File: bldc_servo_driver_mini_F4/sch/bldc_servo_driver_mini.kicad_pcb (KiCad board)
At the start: 4 copper layers, 35 x 40 mm, 68 parts, among them IC1 ST730MR, IC2 LDK320AM50R, IC3 TLT9251VLEXUMA1, J1 1-2328702-0, J2 Conn_01x04, J3 Conn_01x04, J4 Conn_01x06, J5 Conn_01x03, J6 Conn_01x02, J7 DF65-3P-1.7V_21_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

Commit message: fix : [F4sch] generate 5V from DCDC
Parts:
- added C29: 10u, Capacitor_SMD:C_0603_1608Metric, F.Cu at (133.3, 93.2)
- added D9: D_Schottky, Diode_SMD:D_SOD-523, F.Cu at (132.6, 91.5)
- added L2: 4.7u, SamacSys_Parts:LPS3314332MRC, F.Cu at (129.8, 93.0)
- added R19: 30.1k, Resistor_SMD:R_0402_1005Metric, F.Cu at (133.9, 87.9)
- added R20: 10k, Resistor_SMD:R_0402_1005Metric, F.Cu at (132.9, 87.9)
- C15: value 1u -> 10u; footprint Capacitor_SMD:C_0402_1005Metric -> Capacitor_SMD:C_0603_1608Metric; moved to F.Cu
- C6: value 0.1u -> 0.01u; moved to F.Cu
- D2: value D_Schottky -> PMEG6010AESBYL; footprint Diode_SMD:D_SOD-523 -> SamacSys_Parts:PMEG6010AESBYL
- D4, R3: moved to F.Cu
- IC2: value LDK320AM50R -> LT1616ES6#TRMPBF; footprint SamacSys_Parts:SOT95P280X145-5N -> SamacSys_Parts:SOT95P280X90-6N; moved to F.Cu
- moved R14 22.1 mm to (110.8, 87.8)
- moved D8 18.9 mm to (111.3, 88.8), turned to 0 degrees
- moved R1 13.1 mm to (113.2, 91.8)
- moved D1 12.1 mm to (115.2, 93.4), turned to 0 degrees
- moved R3 6.19 mm to (127.2, 87.2), turned to 180 degrees
- moved D4 4.61 mm to (127.0, 92.0)
- moved C6 2.86 mm to (130.8, 90.6)
- moved C15 2.50 mm to (127.2, 89.2), turned to 90 degrees
- moved IC2 2.35 mm to (130.2, 88.4), turned to 180 degrees
- moved D2 1.85 mm to (125.8, 93.8), turned to 270 degrees
- moved D6 1.60 mm to (130.2, 85.6)
- moved R12 1.60 mm to (133.0, 85.6)
- moved D7 1.50 mm to (130.2, 83.7)
- moved R13 1.50 mm to (133.0, 83.7)
- moved R5 0.20 mm to (124.4, 90.6)
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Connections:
- C15 pad 1: +5V -> GND
- C15 pad 2: GND -> Net-(C15-Pad2)
- C6 pad 2: GND -> Net-(C6-Pad2)
- C8 pad 1: Net-(C6-Pad1) -> +5V
- D2 pad 1: Net-(C6-Pad1) -> Net-(C15-Pad2)
- D3 pad 1: Net-(C6-Pad1) -> +5V
- D4 pad 1: Net-(C6-Pad1) -> Net-(C6-Pad2)
- D4 pad 2: +5V -> GND
- IC1 pad 3: Net-(C6-Pad1) -> +5V
- IC2 pad 5: +5V -> Net-(C15-Pad2)
- R3 pad 1: Net-(C6-Pad1) -> Net-(IC2-Pad4)
- R3 pad 2: Net-(IC2-Pad3) -> Net-(C15-Pad2)
- R4 pad 1: Net-(C6-Pad1) -> +5V
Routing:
- net +5V: track 14.9 -> 46.0 mm, vias 0 -> 2
- net Net-(C6-Pad1): track 24.8 -> 2.75 mm, vias 1 -> 0
- net Net-(C15-Pad2): track 0.00 -> 9.02 mm
- net Net-(C6-Pad2): track 0.00 -> 6.95 mm
- net +3V3: track 155.2 -> 150.8 mm
- net /LED1: track 14.2 -> 12.7 mm
- net Net-(IC2-Pad4): track 0.00 -> 1.30 mm
- net Net-(IC2-Pad3): track 1.59 -> 2.45 mm
- net +12V: track 8.23 -> 8.09 mm, vias 14 -> 12
- net GND: vias 74 -> 79
- added copper zone on F.Cu, net +5V

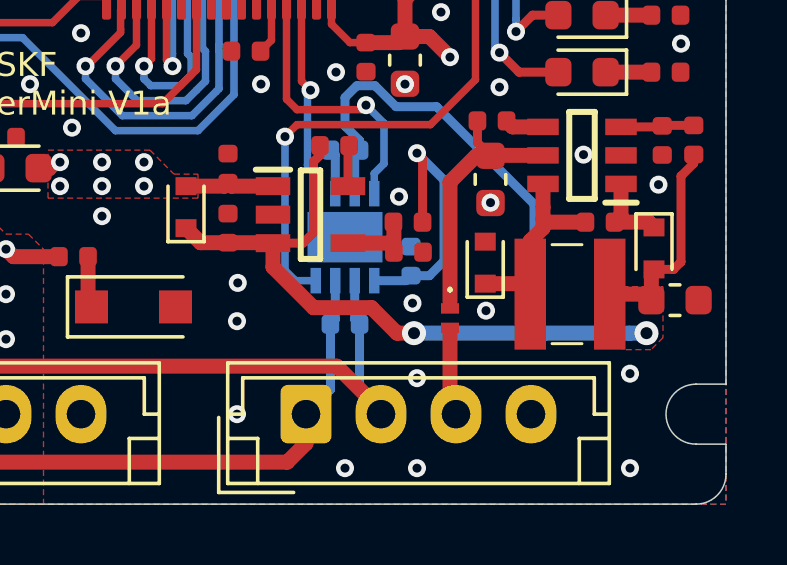
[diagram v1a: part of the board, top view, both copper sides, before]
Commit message: fix : [F4sch] change a diode footprint of 5v line
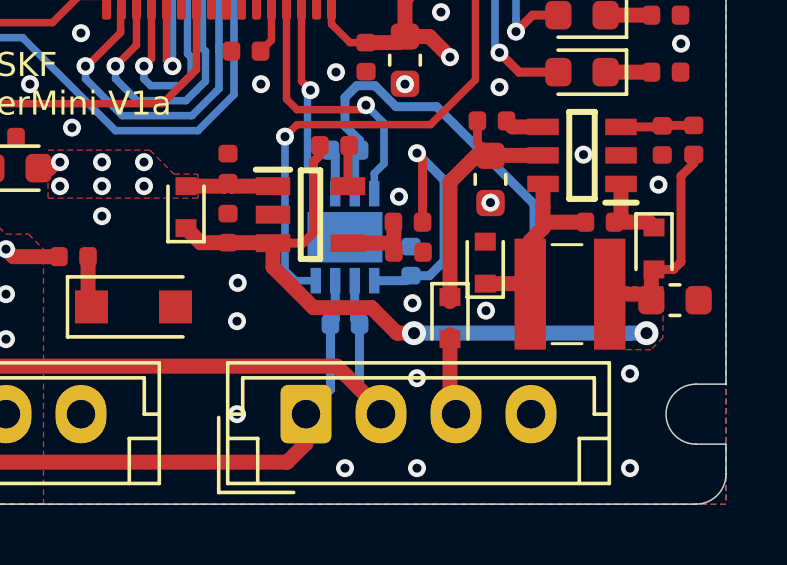
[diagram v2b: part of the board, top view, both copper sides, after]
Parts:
- D2: footprint SamacSys_Parts:PMEG6010AESBYL -> Diode_SMD:D_SOD-523
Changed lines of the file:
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@@
   (general
     (thickness 1.6)
-    (drawings 25)
-    (tracks 914)
+    (drawings 24)
+    (tracks 912)
     (zones 0)
     (modules 73)
@@
     (37 F.SilkS user)
     (38 B.Mask user hide)
-    (39 F.Mask user hide)
+    (39 F.Mask user)
     (40 Dwgs.User user)
     (41 Cmts.User user)
@@
   )
   (setup
-    (last_trace_width 0.5)
+    (last_trace_width 0.25)
     (user_trace_width 0.2)
     (user_trace_width 0.3)
@@
     )
   )
-  (module SamacSys_Parts:PMEG6010AESBYL (layer F.Cu)
-    (at 125.8 93.8 270)
-    (descr "DSN1006-2 (SOD993)_1")
-    (tags "Schottky Diode")
-    (attr smd)
-    (fp_text reference D2 (at 0 0 90) (layer F.SilkS) hide
-      (effects (font (size 1.27 1.27) (thickness 0.254)))
-    )
-    (fp_text value PMEG6010AESBYL (at 0 0 90) (layer F.Fab) hide
-      (effects (font (size 1.27 1.27) (thickness 0.254)))
-    )
-    (fp_text user %R (at 0 0 90) (layer F.Fab) hide
-      (effects (font (size 1.27 1.27) (thickness 0.254)))
-    )
-    (fp_line (start -0.5 -0.3) (end 0.5 -0.3) (layer F.Fab) (width 0.2))
-    (fp_line (start 0.5 -0.3) (end 0.5 0.3) (layer F.Fab) (width 0.2))
-    (fp_line (start 0.5 0.3) (end -0.5 0.3) (layer F.Fab) (width 0.2))
-    (fp_line (start -0.5 0.3) (end -0.5 -0.3) (layer F.Fab) (width 0.2))
-    (fp_line (start -1.5 -1.3) (end 1.5 -1.3) (layer F.CrtYd) (width 0.1))
-    (fp_line (start 1.5 -1.3) (end 1.5 1.3) (layer F.CrtYd) (width 0.1))
-    (fp_line (start 1.5 1.3) (end -1.5 1.3) (layer F.CrtYd) (width 0.1))
-    (fp_line (start -1.5 1.3) (end -1.5 -1.3) (layer F.CrtYd) (width 0.1))
-    (fp_line (start -1 0) (end -1 0) (layer F.SilkS) (width 0.1))
-    (fp_line (start -0.9 0) (end -0.9 0) (layer F.SilkS) (width 0.1))
-    (fp_arc (start -0.95 0) (end -1 0) (angle -180) (layer F.SilkS) (width 0.1))
-    (fp_arc (start -0.95 0) (end -0.9 0) (angle -180) (layer F.SilkS) (width 0.1))
-    (pad 1 smd rect (at -0.325 0 270) (size 0.35 0.6) (layers F.Cu F.Paste F.Mask)
-      (net 86 "Net-(C15-Pad2)"))
-    (pad 2 smd rect (at 0.325 0 270) (size 0.35 0.6) (layers F.Cu F.Paste F.Mask)
-      (net 12 +12V))
-  )
   (module Diode_SMD:D_SOD-523 (layer F.Cu)
     (at 126.975 91.95 90)
@@
     )
   )
-  (gr_line (start 125.8 92.9) (end 125.8 94.75) (layer F.Mask) (width 0.5))
+  (module Diode_SMD:D_SOD-523 (layer F.Cu)
+    (at 125.8 93.8 270)
+    (descr "http://www.diodes.com/datasheets/ap02001.pdf p.144")
+    (tags "Diode SOD523")
+    (attr smd)
+    (fp_text reference D2 (at 0 -1.3 90) (layer F.SilkS) hide
+      (effects (font (size 1 1) (thickness 0.15)))
+    )
+    (fp_text value PMEG6010AESBYL (at 0 1.4 90) (layer F.Fab) hide
+      (effects (font (size 1 1) (thickness 0.15)))
+    )
+    (fp_text user %R (at 0 -1.3 90) (layer F.Fab) hide
+      (effects (font (size 1 1) (thickness 0.15)))
+    )
+    (fp_line (start -1.15 -0.6) (end -1.15 0.6) (layer F.SilkS) (width 0.12))
+    (fp_line (start 1.25 -0.7) (end 1.25 0.7) (layer F.CrtYd) (width 0.05))
+    (fp_line (start -1.25 -0.7) (end 1.25 -0.7) (layer F.CrtYd) (width 0.05))
+    (fp_line (start -1.25 0.7) (end -1.25 -0.7) (layer F.CrtYd) (width 0.05))
+    (fp_line (start 1.25 0.7) (end -1.25 0.7) (layer F.CrtYd) (width 0.05))
+    (fp_line (start 0.1 0) (end 0.25 0) (layer F.Fab) (width 0.1))
+    (fp_line (start 0.1 -0.2) (end -0.2 0) (layer F.Fab) (width 0.1))
+    (fp_line (start 0.1 0.2) (end 0.1 -0.2) (layer F.Fab) (width 0.1))
+    (fp_line (start -0.2 0) (end 0.1 0.2) (layer F.Fab) (width 0.1))
+    (fp_line (start -0.2 0) (end -0.35 0) (layer F.Fab) (width 0.1))
+    (fp_line (start -0.2 0.2) (end -0.2 -0.2) (layer F.Fab) (width 0.1))
+    (fp_line (start 0.65 -0.45) (end 0.65 0.45) (layer F.Fab) (width 0.1))
+    (fp_line (start -0.65 -0.45) (end 0.65 -0.45) (layer F.Fab) (width 0.1))
+    (fp_line (start -0.65 0.45) (end -0.65 -0.45) (layer F.Fab) (width 0.1))
+    (fp_line (start 0.65 0.45) (end -0.65 0.45) (layer F.Fab) (width 0.1))
+    (fp_line (start 0.7 -0.6) (end -1.15 -0.6) (layer F.SilkS) (width 0.12))
+    (fp_line (start 0.7 0.6) (end -1.15 0.6) (layer F.SilkS) (width 0.12))
+    (pad 2 smd rect (at 0.7 0 90) (size 0.6 0.7) (layers F.Cu F.Paste F.Mask)
+      (net 12 +12V))
+    (pad 1 smd rect (at -0.7 0 90) (size 0.6 0.7) (layers F.Cu F.Paste F.Mask)
+      (net 86 "Net-(C15-Pad2)"))
+    (model ${KISYS3DMOD}/Diode_SMD.3dshapes/D_SOD-523.wrl
+      (at (xyz 0 0 0))
+      (scale (xyz 1 1 1))
+      (rotate (xyz 0 0 0))
+    )
+  )
   (gr_line (start 123.7 91.4) (end 124.15 91.4) (layer B.Mask) (width 0.8))
   (gr_text Ptnt (at 127.6 67.4 90) (layer F.SilkS)
@@
   (segment (start 131.5 90.385) (end 131.285 90.6) (width 0.5) (layer F.Cu) (net 6))
   (segment (start 131.5 89.325) (end 131.5 90.385) (width 0.5) (layer F.Cu) (net 6))
+  (segment (start 126.665 75.15) (end 126.7 75.115) (width 0.3) (layer F.Cu) (net 7))
+  (segment (start 123.775 75.15) (end 126.665 75.15) (width 0.3) (layer F.Cu) (net 7))
+  (segment (start 126.7 75.115) (end 127.7 75.115) (width 0.3) (layer F.Cu) (net 7))
+  (segment (start 128.985 75.115) (end 129 75.1) (width 0.3) (layer F.Cu) (net 7))
+  (segment (start 127.7 75.115) (end 128.985 75.115) (width 0.3) (layer F.Cu) (net 7))
   (segment (start 117.485 91.285) (end 117 90.8) (width 0.5) (layer F.Cu) (net 8))
   (segment (start 118.4 91.285) (end 117.485 91.285) (width 0.5) (layer F.Cu) (net 8))
@@
   (segment (start 120.9 91.3) (end 119.9 91.3) (width 0.3) (layer F.Cu) (net 8))
   (segment (start 121.25 90.95) (end 120.9 91.3) (width 0.3) (layer F.Cu) (net 8))
-  (segment (start 126.665 75.15) (end 126.7 75.115) (width 0.3) (layer F.Cu) (net 7))
-  (segment (start 123.775 75.15) (end 126.665 75.15) (width 0.3) (layer F.Cu) (net 7))
-  (segment (start 126.7 75.115) (end 127.7 75.115) (width 0.3) (layer F.Cu) (net 7))
-  (segment (start 128.985 75.115) (end 129 75.1) (width 0.3) (layer F.Cu) (net 7))
-  (segment (start 127.7 75.115) (end 128.985 75.115) (width 0.3) (layer F.Cu) (net 7))
   (segment (start 122.625 88.36) (end 122.785 88.2) (width 0.3) (layer B.Cu) (net 8))
   (segment (start 122.625 89.65) (end 122.625 88.36) (width 0.3) (layer B.Cu) (net 8))
@@
   (segment (start 111.25 91.75) (end 111 91.5) (width 0.5) (layer F.Cu) (net 12))
   (segment (start 112.765 91.75) (end 111.25 91.75) (width 0.5) (layer F.Cu) (net 12))
-  (segment (start 125.8 94.125) (end 125.8 94.35) (width 0.3) (layer F.Cu) (net 12))
   (segment (start 125.8 96.8) (end 126 97) (width 0.5) (layer F.Cu) (net 12))
   (segment (start 125.8 94.35) (end 125.8 96.8) (width 0.5) (layer F.Cu) (net 12))
@@
   (segment (start 126.715 87.9525) (end 127.15 88.3875) (width 0.3) (layer F.Cu) (net 86))
   (segment (start 126.715 87.225) (end 126.715 87.9525) (width 0.3) (layer F.Cu) (net 86))
-  (segment (start 125.8 93.475) (end 125.8 93.25) (width 0.3) (layer F.Cu) (net 86))
   (segment (start 126.675 88.3875) (end 127.15 88.3875) (width 0.5) (layer F.Cu) (net 86))
   (segment (start 125.8 89.2625) (end 126.675 88.3875) (width 0.5) (layer F.Cu) (net 86))
